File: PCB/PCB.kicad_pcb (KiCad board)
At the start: 6 copper layers, 255 x 147 mm, 163 parts, among them IC1 S25FL256LAGMFI003, IC2 LT1932ES6#TRMPBF, J1 0878311420, J2 USB_B_Micro, J4 62684-402100ALF, J5 L77HDE15SD1CH4FVGA, J6 USB1130-15-A_REVA, SW1 SW_Push, SW2 SW_Push, SW3 SW_Push, SW4 SW_Push, U1 TPS54325, U2 TPS54294, U3 COM-09032, U4 XC7A100T-FTG256, U5 IS62C1024AL-35QLI-TR, Y1 Crystal_GND24, Y2 ECS-3953M-400-BN-TR

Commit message: ....
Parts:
- C48, C49, C50, C51, C52, C53, C54, C55, C56, C58, C59, C60, C61, C62, C63, C64, C65, C66, C67, C68, C69, C70, C71, C72, C73, C74, C75, C76, C77, C78, C79, C80, C81, C82, C83, C84: moved to B.Cu
- moved C56 30.1 mm to (229.2, 46.2), turned to 0 degrees
- moved C58 30.1 mm to (229.2, 43.2), turned to 0 degrees
- moved C59 30.1 mm to (229.2, 40.2), turned to 0 degrees
- moved C60 30.1 mm to (229.2, 37.2), turned to 0 degrees
- moved C61 30.1 mm to (229.2, 34.2), turned to 0 degrees
- moved C62 30.1 mm to (229.2, 31.2), turned to 0 degrees
- moved C63 30.1 mm to (229.2, 28.2), turned to 0 degrees
- moved C78 30.1 mm to (199.1, 29.2), turned to 180 degrees
- moved C79 30.1 mm to (199.1, 32.3), turned to 180 degrees
- moved C80 30.1 mm to (199.1, 35.2), turned to 180 degrees
- moved C81 30.1 mm to (199.1, 38.4), turned to 180 degrees
- moved C82 30.1 mm to (199.1, 41.2), turned to 180 degrees
- moved C83 30.1 mm to (199.1, 44.2), turned to 180 degrees
- moved C84 30.1 mm to (199.1, 47.3), turned to 180 degrees
- moved C55 29.4 mm to (228.9, 51.2), turned to 180 degrees
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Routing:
- net /FPGA/RED4: track 0.00 -> 77.4 mm
- net /FPGA/RED2: track 0.71 -> 76.2 mm, vias 1 -> 4
- net /FPGA/RED3: track 0.00 -> 75.2 mm
- net /FPGA/GREEN4: track 0.71 -> 75.3 mm, vias 1 -> 4
- net /FPGA/HSYNC: track 0.00 -> 73.5 mm, vias 0 -> 2
- net /FPGA/VSYNC: track 0.71 -> 73.5 mm, vias 1 -> 2
- net Net-(IC1-SCK): track 0.71 -> 71.9 mm, vias 1 -> 2
- net /FPGA/RED1: track 0.71 -> 68.5 mm, vias 1 -> 2
- net /FPGA/BLUE0: track 0.71 -> 67.1 mm, vias 1 -> 2
- net Net-(IC1-SO_/_IO1): track 0.71 -> 66.7 mm, vias 1 -> 2
- net /FPGA/RED0: track 0.71 -> 65.9 mm, vias 1 -> 2
- net Net-(U4B-IO_L22P_T3_35): track 0.00 -> 62.2 mm, vias 0 -> 2
- net Net-(IC1-CS#): track 0.71 -> 62.5 mm, vias 1 -> 2
- net /FPGA/GREEN3: track 1.36 -> 61.1 mm, vias 0 -> 2
- net /FPGA/GREEN2: track 1.24 -> 59.7 mm, vias 0 -> 2
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
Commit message: push<
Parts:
- moved C24 225.1 mm to (229.8, 20.3)
- moved C25 225.1 mm to (229.8, 23.3)
- moved C26 225.1 mm to (229.8, 26.3)
- moved C27 225.1 mm to (229.8, 29.3)
- moved C28 225.1 mm to (229.8, 32.3)
- moved C29 225.1 mm to (229.8, 35.3)
- moved C30 225.1 mm to (229.8, 38.3)
- moved C31 225.1 mm to (229.8, 41.3)
- moved C32 225.1 mm to (229.8, 44.3)
- moved C33 225.1 mm to (229.8, 47.3)
- moved C34 225.1 mm to (229.8, 50.4)
- moved C35 225.1 mm to (229.8, 53.7)
- moved C36 225.1 mm to (229.8, 56.7)
- moved C37 225.1 mm to (229.8, 59.7)
- moved C38 225.1 mm to (229.8, 62.8)
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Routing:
- net Net-(U4B-IO_L17N_T2_35): track 0.00 -> 79.1 mm, vias 0 -> 2
- net Net-(U4B-IO_L20P_T3_35): track 0.00 -> 77.5 mm, vias 0 -> 2
- net Net-(U4B-IO_L20N_T3_35): track 0.00 -> 69.7 mm, vias 0 -> 2
- net Net-(U4B-IO_L19P_T3_35): track 0.71 -> 67.7 mm, vias 1 -> 2
- net Net-(U4B-IO_L18N_T2_35): track 0.71 -> 65.9 mm, vias 1 -> 2
- net Net-(U4B-IO_L21P_T3_DQS_35): track 3.32 -> 67.8 mm, vias 1 -> 2
- net Net-(U4B-IO_L17P_T2_35): track 0.00 -> 61.5 mm, vias 0 -> 2
- net Net-(U4B-IO_L21N_T3_DQS_35): track 0.71 -> 60.1 mm, vias 1 -> 2
- net Net-(U4B-IO_L16N_T2_35): track 0.71 -> 58.3 mm, vias 1 -> 2
- net Net-(U4B-IO_L18P_T2_35): track 0.71 -> 54.4 mm, vias 1 -> 2
- net Net-(U4B-IO_L12P_T1_MRCC_35): track 0.71 -> 12.3 mm, vias 1 -> 0
- net Net-(U4B-IO_L15N_T2_DQS_35): track 0.00 -> 10.3 mm
- net Net-(U4B-IO_L10N_T1_AD15N_35): track 0.00 -> 8.43 mm
- net Net-(U4B-IO_L9P_T1_DQS_AD7P_35): track 0.00 -> 7.35 mm
- net GND: track 422.8 -> 430.0 mm, vias 167 -> 171
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
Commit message: FPGA Done?
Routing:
- net Net-(U4A-IO_L11N_T1_SRCC_15): track 0.00 -> 96.1 mm, vias 0 -> 2
- net Net-(U4A-IO_L14N_T2_SRCC_15): track 0.71 -> 89.6 mm, vias 1 -> 2
- net Net-(U4A-IO_L12P_T1_MRCC_15): track 0.71 -> 89.1 mm, vias 1 -> 2
- net Net-(U4A-IO_L14P_T2_SRCC_15): track 0.71 -> 86.1 mm, vias 1 -> 2
- net Net-(U4A-IO_L15P_T2_DQS_15): track 0.00 -> 83.6 mm, vias 0 -> 2
- net Net-(U4A-IO_L19N_T3_A21_VREF_15): track 0.71 -> 82.0 mm, vias 1 -> 3
- net Net-(U4A-IO_L20N_T3_A19_15): track 0.71 -> 79.8 mm, vias 1 -> 2
- net Net-(U4A-IO_L13N_T2_MRCC_15): track 1.71 -> 75.7 mm, vias 1 -> 2
- net Net-(U4A-IO_L11P_T1_SRCC_15): track 0.71 -> 74.3 mm, vias 1 -> 2
- net Net-(U4A-IO_L20P_T3_A20_15): track 0.71 -> 71.0 mm, vias 1 -> 2
- net Net-(U4A-IO_25_15): track 0.71 -> 70.9 mm, vias 1 -> 3
- net Net-(U4A-IO_L21P_T3_DQS_15): track 0.71 -> 67.6 mm, vias 1 -> 2
- net Net-(U4A-IO_L13P_T2_MRCC_15): track 0.00 -> 66.2 mm, vias 0 -> 2
- net Net-(U4A-IO_L12N_T1_MRCC_15): track 1.71 -> 66.2 mm, vias 1 -> 2
- net Net-(U4A-IO_L16P_T2_A28_15): track 0.71 -> 63.9 mm, vias 1 -> 2
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
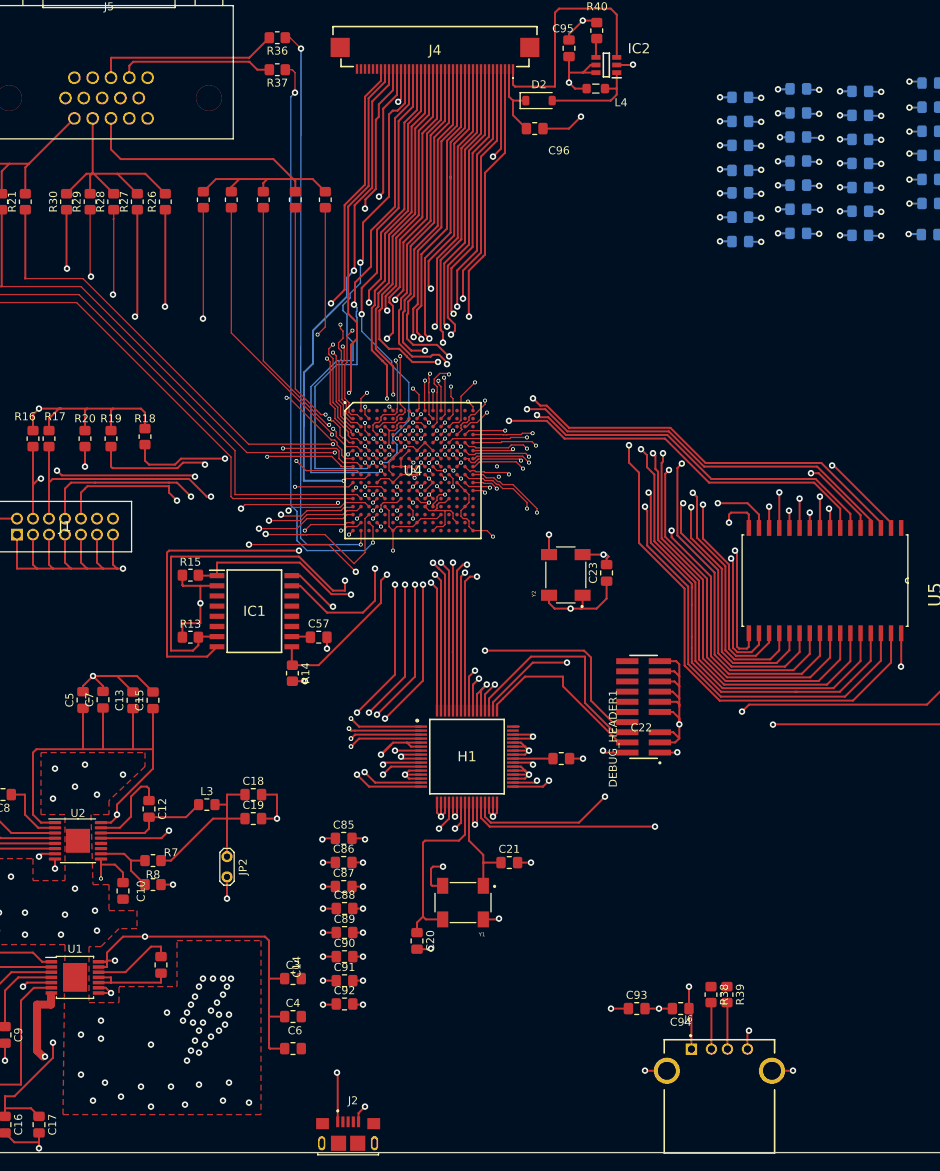
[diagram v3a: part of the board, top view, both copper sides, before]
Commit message: Error handling and line management
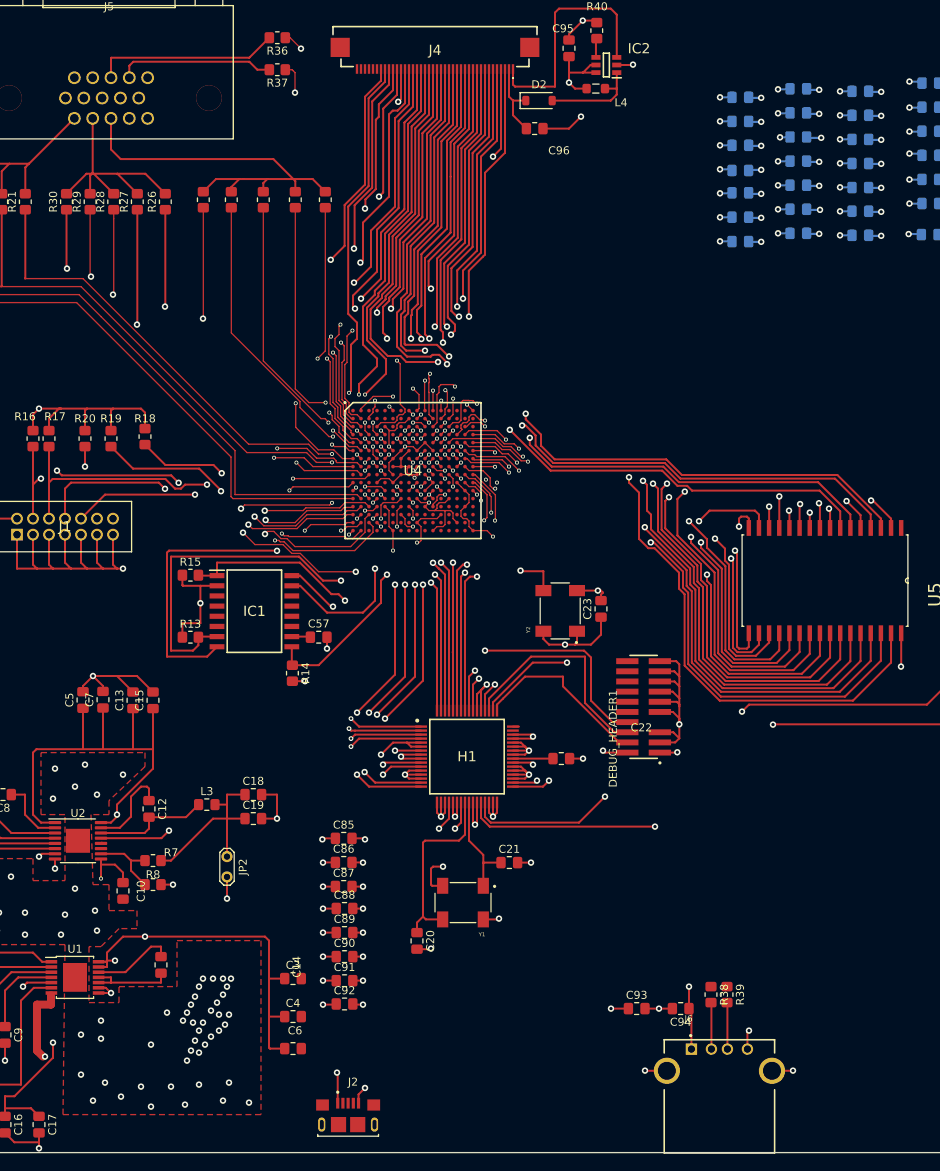
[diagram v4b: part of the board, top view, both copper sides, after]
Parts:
- moved C23 4.55 mm to (173.0, 96.8)
- moved Y2 4.55 mm to (167.9, 97.0)
- moved J2 2.33 mm to (141.4, 161.2)
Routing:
- net Net-(U4C-TDI_0): track 57.9 -> 46.4 mm
- net Net-(U4C-TCK_0): track 68.6 -> 59.3 mm
- net GND: track 442.3 -> 435.6 mm, vias 173 -> 174
- net Net-(U4A-IO_L12P_T1_MRCC_15): track 89.1 -> 83.1 mm
- net /FPGA/BLUE0: track 67.0 -> 61.2 mm
- net Net-(U4A-IO_L19P_T3_A22_15): track 49.2 -> 53.8 mm
- net Net-(U4A-IO_L11N_T1_SRCC_15): track 96.1 -> 91.5 mm
- net Net-(U4A-IO_L14N_T2_SRCC_15): track 89.6 -> 85.2 mm
- net Net-(U4A-IO_L14P_T2_SRCC_15): track 86.1 -> 81.8 mm
- net Net-(U4A-IO_L15P_T2_DQS_15): track 83.6 -> 79.5 mm
- net Net-(U4A-IO_L13P_T2_MRCC_14): track 25.2 -> 21.3 mm
- net Net-(U4B-IO_L18P_T2_35): track 57.3 -> 61.1 mm
- net Net-(U4A-IO_L16N_T2_A27_15): track 61.6 -> 58.1 mm
- net /FPGA/VSYNC: track 73.5 -> 76.8 mm
- net Net-(U4A-IO_L16P_T2_A28_15): track 63.9 -> 60.8 mm
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
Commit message: Finish PCB
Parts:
- added L2: 1.5u, Inductor_SMD:L_0805_2012Metric_Pad1.15x1.40mm_HandSolder, F.Cu at (120.2, 140.8)
- C24, C25, C26, C27, C28, C29, C30, C31, C32, C33, C34, C35, C36, C37, C38, C39, C40, C41, C42, C43, C44, C45, C46, C47: moved to B.Cu
- moved C42 146.7 mm to (122.3, 112.5), turned to -90 degrees
- moved C43 142.5 mm to (125.3, 112.5), turned to -90 degrees
- moved C44 138.3 mm to (128.3, 112.5), turned to -90 degrees
- moved C45 134.2 mm to (131.3, 112.5), turned to -90 degrees
- moved C46 130.0 mm to (134.3, 112.5), turned to -90 degrees
- moved C39 126.3 mm to (119.0, 64.0), turned to 90 degrees
- moved C47 125.9 mm to (137.3, 112.5), turned to -90 degrees
- moved C40 122.8 mm to (122.2, 64.0), turned to 90 degrees
- moved C41 119.2 mm to (125.8, 64.0), turned to 90 degrees
- moved C31 112.6 mm to (122.0, 74.0), turned to 180 degrees
- moved C32 112.3 mm to (122.0, 76.0), turned to 180 degrees
- moved C25 108.4 mm to (126.2, 55.5), turned to 180 degrees
- moved C26 108.2 mm to (126.3, 57.8), turned to 180 degrees
- moved C35 108.1 mm to (123.0, 70.5), turned to -90 degrees
- moved C27 108.0 mm to (126.3, 60.0), turned to 180 degrees
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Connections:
- net Net-(H1-PF10) renamed /microcontroller_unit/D-
- net Net-(H1-PF11) renamed /microcontroller_unit/D+
- net Net-(J6-D+) renamed /microcontroller_unit/D1+
- net Net-(J6-D-) renamed /microcontroller_unit/D1-
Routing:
- net +1V0: track 11.4 -> 230.7 mm, vias 3 -> 5
- net +1V8: track 4.30 -> 120.9 mm
- net GND: track 435.6 -> 544.6 mm, vias 174 -> 200
- net /microcontroller_unit/D+: track 0.76 -> 46.3 mm
- net /microcontroller_unit/D-: track 0.00 -> 44.8 mm
- net Net-(U2-EN2): track 16.5 -> 42.8 mm, vias 0 -> 2
- net Net-(JP1-A): track 55.1 -> 71.1 mm, vias 2 -> 3
- net +3.3V: track 300.3 -> 304.4 mm, vias 87 -> 89
- net Net-(H1-DECOUPLE): track 5.01 -> 8.52 mm
- net Net-(IC2-LED): track 30.1 -> 32.7 mm
- net Net-(D2-A): track 12.6 -> 15.1 mm
- net Net-(U1-SW1): track 11.2 -> 13.6 mm
- net /FPGA/program_b: track 94.4 -> 96.4 mm
- net Net-(U4A-IO_L11P_T1_SRCC_15): track 72.0 -> 73.2 mm
- net /microcontroller_unit/D1+: track 5.83 -> 6.55 mm
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
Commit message: Small fixes
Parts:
- moved D2 9.53 mm to (174.8, 34.0)
- moved J5 3.64 mm to (111.4, 17.9)
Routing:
- net Net-(D2-K): track 9.95 -> 19.5 mm
- net Net-(D2-A): track 15.1 -> 6.82 mm
- net Net-(IC2-LED): track 32.7 -> 38.9 mm
- net GND: track 544.6 -> 540.0 mm, vias 200 -> 217
- net Net-(J5-Pad3): track 50.2 -> 53.9 mm
- net Net-(J5-Pad1): track 39.2 -> 42.8 mm
- net Net-(J5-Pad2): track 31.2 -> 34.7 mm
- net Net-(J5-Pad13): track 23.3 -> 21.5 mm
- net Net-(J5-Pad14): track 19.6 -> 20.5 mm
